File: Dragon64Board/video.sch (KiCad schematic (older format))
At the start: 69 parts, among them IC10 6847, IC12 74LS393, IC13 74LS32, IC14 74LS74, IC17 LM1889N, IC18 74LS86, IC19 74LS00, IC23 74LS393, IC24 74LS390, IC28 LM318N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

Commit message: PAL to NTSC
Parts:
- removed C20, C33, C44: 4.7uf tant, Capacitor_THT:CP_Radial_D4.0mm_P2.00mm, symbol Device:C_Polarized_US
- removed C32: 2-22p, dragon64:C_Trimmer_D7.5mm, symbol Device:C_Variable
- removed C36: 180p, Capacitor_THT:C_Disc_D7.5mm_W2.5mm_P5.00mm, symbol Device:C
- removed C48: .01u, Capacitor_THT:C_Disc_D7.5mm_W2.5mm_P5.00mm, symbol Device:C
- removed C49: 4p7, Capacitor_THT:C_Disc_D7.5mm_W2.5mm_P5.00mm, symbol Device:C
- removed C54: 330p, Capacitor_THT:C_Disc_D7.5mm_W2.5mm_P5.00mm, symbol Device:C
- removed D21, D22: 1N4148, Diode_THT:D_DO-35_SOD27_P7.62mm_Horizontal, symbol Device:D
- removed IC12, IC23: 74LS393, Package_DIP:DIP-14_W7.62mm_Socket_LongPads, symbol 74xx:74LS393
- removed IC13: 74LS32, Package_DIP:DIP-14_W7.62mm_Socket_LongPads, symbol 74xx:74LS32
- removed IC14, IC30: 74LS74, Package_DIP:DIP-14_W7.62mm_Socket_LongPads, symbol 74xx:74LS74
- removed IC17: LM1889N, Package_DIP:DIP-18_W7.62mm_Socket_LongPads, symbol dragon64:LM1889N
- removed IC18: 74LS86, Package_DIP:DIP-14_W7.62mm_Socket_LongPads, symbol 74xx:74LS86
- removed IC19: 74LS00, Package_DIP:DIP-14_W7.62mm_Socket_LongPads, symbol 74xx:74LS00
- removed IC24: 74LS390, Package_DIP:DIP-16_W7.62mm_Socket_LongPads, symbol 74xx:74LS390
- removed IC28: LM318N, Package_DIP:DIP-8_W7.62mm_Socket_LongPads, symbol Amplifier_Operational:LM318N
- removed IC29: 4053, Package_DIP:DIP-16_W7.62mm_Socket_LongPads, symbol dragon64:4053
- removed IC31: 74LS123, Package_DIP:DIP-16_W7.62mm_Socket_LongPads, symbol 74xx:74LS123
- removed IC9: 74LS20, Package_DIP:DIP-14_W7.62mm_Socket_LongPads, symbol 74xx:74LS20
- removed LK2: ~, Connector_PinHeader_2.54mm:PinHeader_1x03_P2.54mm_Vertical, symbol Jumper:Jumper_3_Bridged12
- removed R41, R58: 1K2, Resistor_THT:R_Axial_DIN0207_L6.3mm_D2.5mm_P7.62mm_Horizontal, symbol Device:R
- removed R42: 5K6, Resistor_THT:R_Axial_DIN0207_L6.3mm_D2.5mm_P7.62mm_Horizontal, symbol Device:R
- removed R43: 10R, Resistor_THT:R_Axial_DIN0207_L6.3mm_D2.5mm_P7.62mm_Horizontal, symbol Device:R
- removed R44: 680R, Resistor_THT:R_Axial_DIN0207_L6.3mm_D2.5mm_P7.62mm_Horizontal, symbol Device:R
- removed R45, R50, R51: 1K, Resistor_THT:R_Axial_DIN0207_L6.3mm_D2.5mm_P7.62mm_Horizontal, symbol Device:R
- removed R46: 270R, Resistor_THT:R_Axial_DIN0207_L6.3mm_D2.5mm_P7.62mm_Horizontal, symbol Device:R
- removed R47: 470R, Resistor_THT:R_Axial_DIN0207_L6.3mm_D2.5mm_P7.62mm_Horizontal, symbol Device:R
- removed R48: 220R, Resistor_THT:R_Axial_DIN0207_L6.3mm_D2.5mm_P7.62mm_Horizontal, symbol Device:R
- removed R49: 330R, Resistor_THT:R_Axial_DIN0207_L6.3mm_D2.5mm_P7.62mm_Horizontal, symbol Device:R
- removed R52, R57: 3K3, Resistor_THT:R_Axial_DIN0207_L6.3mm_D2.5mm_P7.62mm_Horizontal, symbol Device:R
- removed R53, R56: 2K7, Resistor_THT:R_Axial_DIN0207_L6.3mm_D2.5mm_P7.62mm_Horizontal, symbol Device:R
- removed R54, R55: 10K, Resistor_THT:R_Axial_DIN0207_L6.3mm_D2.5mm_P7.62mm_Horizontal, symbol Device:R
- removed R59: 6K8, Resistor_THT:R_Axial_DIN0207_L6.3mm_D2.5mm_P7.62mm_Horizontal, symbol Device:R
- removed R60: 15K, Resistor_THT:R_Axial_DIN0207_L6.3mm_D2.5mm_P7.62mm_Horizontal, symbol Device:R
- removed R61: 1K8, Resistor_THT:R_Axial_DIN0207_L6.3mm_D2.5mm_P7.62mm_Horizontal, symbol Device:R
- removed R62: 8K2, Resistor_THT:R_Axial_DIN0207_L6.3mm_D2.5mm_P7.62mm_Horizontal, symbol Device:R
- removed R63: 12K, Resistor_THT:R_Axial_DIN0207_L6.3mm_D2.5mm_P7.62mm_Horizontal, symbol Device:R
- removed R72: 22K, Resistor_THT:R_Axial_DIN0207_L6.3mm_D2.5mm_P7.62mm_Horizontal, symbol Device:R
- removed TR2, TR3: 2N2369A, Package_TO_SOT_THT:TO-18-3, symbol Device:Q_NPN_EBC
- removed TR4: BC212L, Package_TO_SOT_THT:TO-92, symbol Device:Q_PNP_ECB
- removed VR1: 10k, Potentiometer_THT:Potentiometer_Vishay_T7-YA_Single_Vertical, symbol Device:R_Potentiometer
- removed Y3: 4.433619Mhz, Crystal:Crystal_HC49-U_Vertical, symbol Device:Crystal
- added C20, C32: .01u, Capacitor_THT:C_Disc_D7.5mm_W2.5mm_P5.00mm, symbol Device:C
- added C33: 0.1uf, Capacitor_THT:C_Disc_D7.5mm_W2.5mm_P5.00mm, symbol Device:C
- added C36: 100uf, Capacitor_THT:CP_Radial_D4.0mm_P2.00mm, symbol Device:C_Polarized_US
- added C44: 470pf, Capacitor_THT:C_Disc_D7.5mm_W2.5mm_P5.00mm, symbol Device:C
- added D4: 1N4002, Diode_THT:D_DO-35_SOD27_P7.62mm_Horizontal, symbol Device:D
- added J3: composite on luma, Connector_PinHeader_2.54mm:PinHeader_1x02_P2.54mm_Vertical, symbol Connector:Conn_01x02_Male
- added Q1: BC557, Package_TO_SOT_THT:TO-92_Wide, symbol Device:Q_PNP_BCE
- added Q2, Q3: 2N2222, Package_TO_SOT_THT:TO-18-3, symbol Device:Q_NPN_BCE
- added R11: 10K, Resistor_THT:R_Axial_DIN0207_L6.3mm_D2.5mm_P7.62mm_Horizontal, symbol Device:R
- added R12, R7: 390, Resistor_THT:R_Axial_DIN0207_L6.3mm_D2.5mm_P7.62mm_Horizontal, symbol Device:R
- added R13: 820, Resistor_THT:R_Axial_DIN0207_L6.3mm_D2.5mm_P7.62mm_Horizontal, symbol Device:R
- added R30: 420, Resistor_THT:R_Axial_DIN0207_L6.3mm_D2.5mm_P7.62mm_Horizontal, symbol Device:R
- added R31, R6: 470, Resistor_THT:R_Axial_DIN0207_L6.3mm_D2.5mm_P7.62mm_Horizontal, symbol Device:R
- added R8: 5.6k, Resistor_THT:R_Axial_DIN0207_L6.3mm_D2.5mm_P7.62mm_Horizontal, symbol Device:R
- added U2: MC1372, Package_DIP:DIP-14_W7.62mm_LongPads, symbol New_Library:MC1372
- C21: value 3p3 -> .01u
- C29, C31: value 33p -> .01u
- C30: value .1u -> 56pf
- C35: value 180p -> 25uf
- C37: value 180p -> 390pf
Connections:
- net labels added: CHROMA, DA0, FS, HS, LUMA, VCLK1
- net labels removed: -5V, CMP, DA0', E, MOD, VID+5V, VIDEO, ~FS, ~HS, ~NHS
- wire segments 439 -> 143
- no-connect marks 41 -> 18
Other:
- note removed: "*"
- note removed: "LINE PULSES"
- note removed: "TANT"
- moved on the sheet: C34, C38, C41, C45, C50, C51

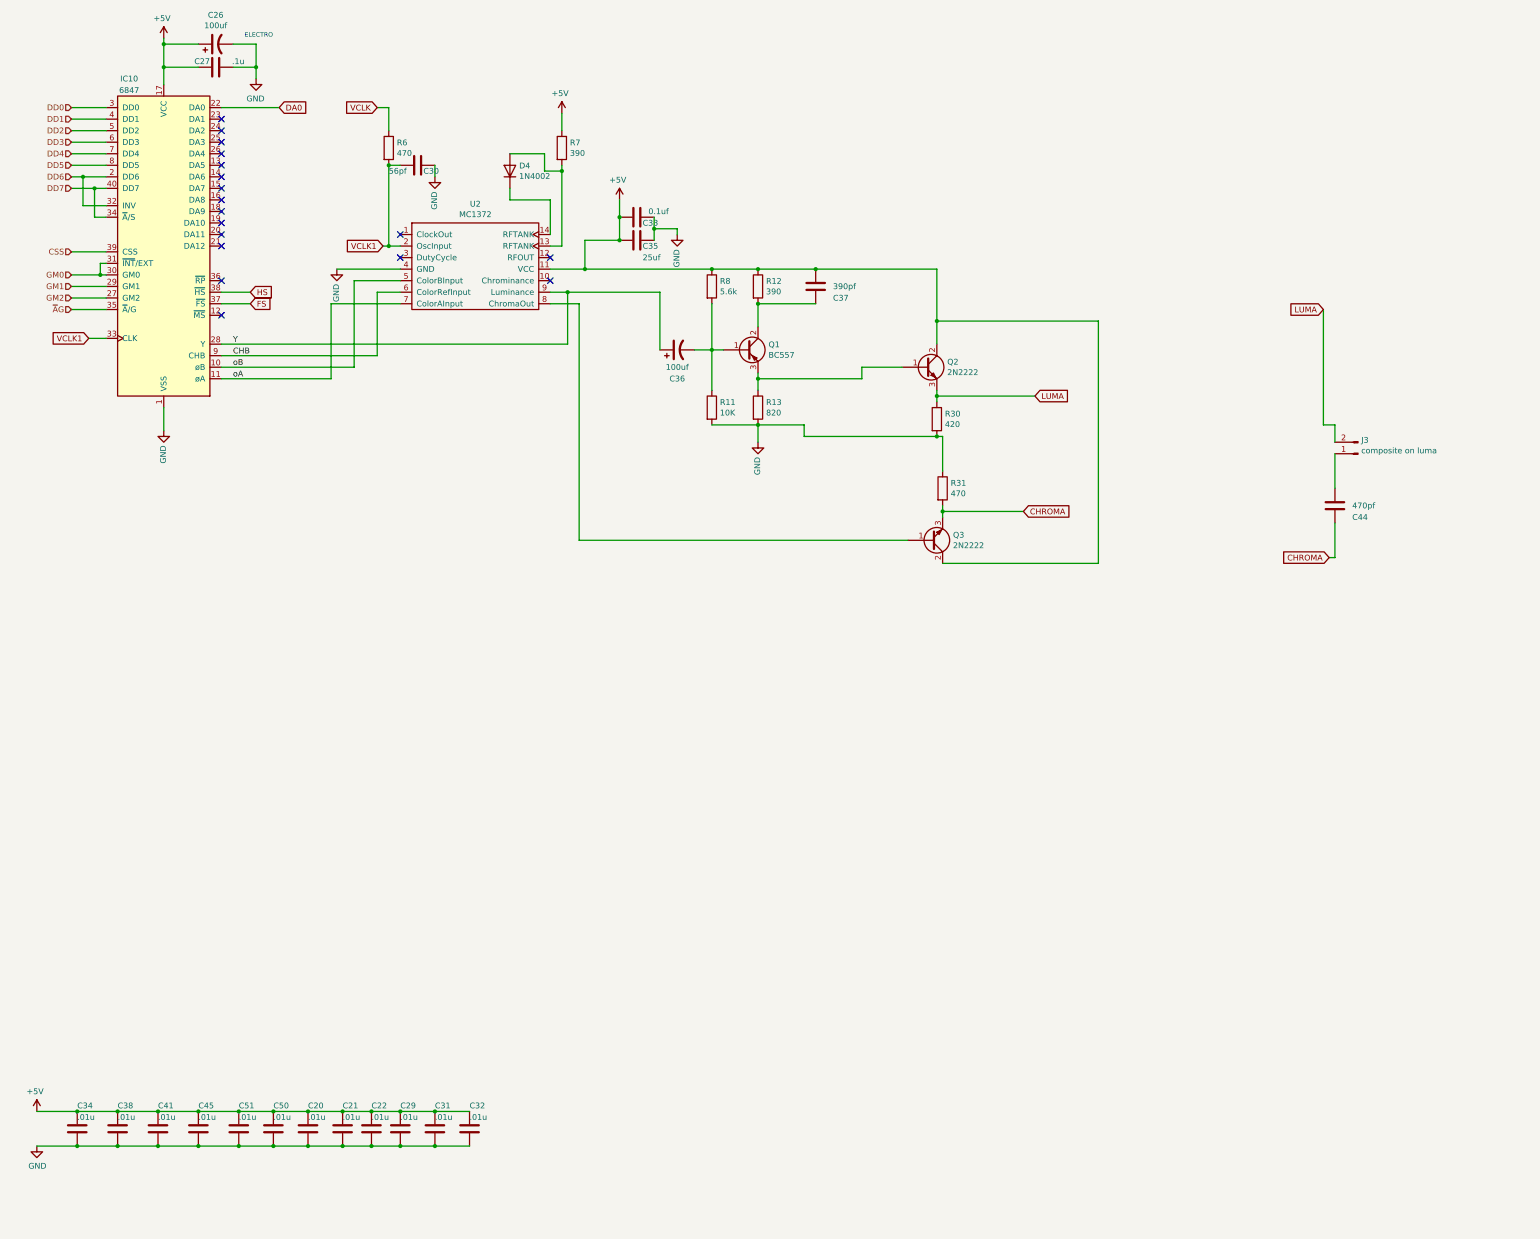
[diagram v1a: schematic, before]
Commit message: Bug fixes and add Floppy Controller
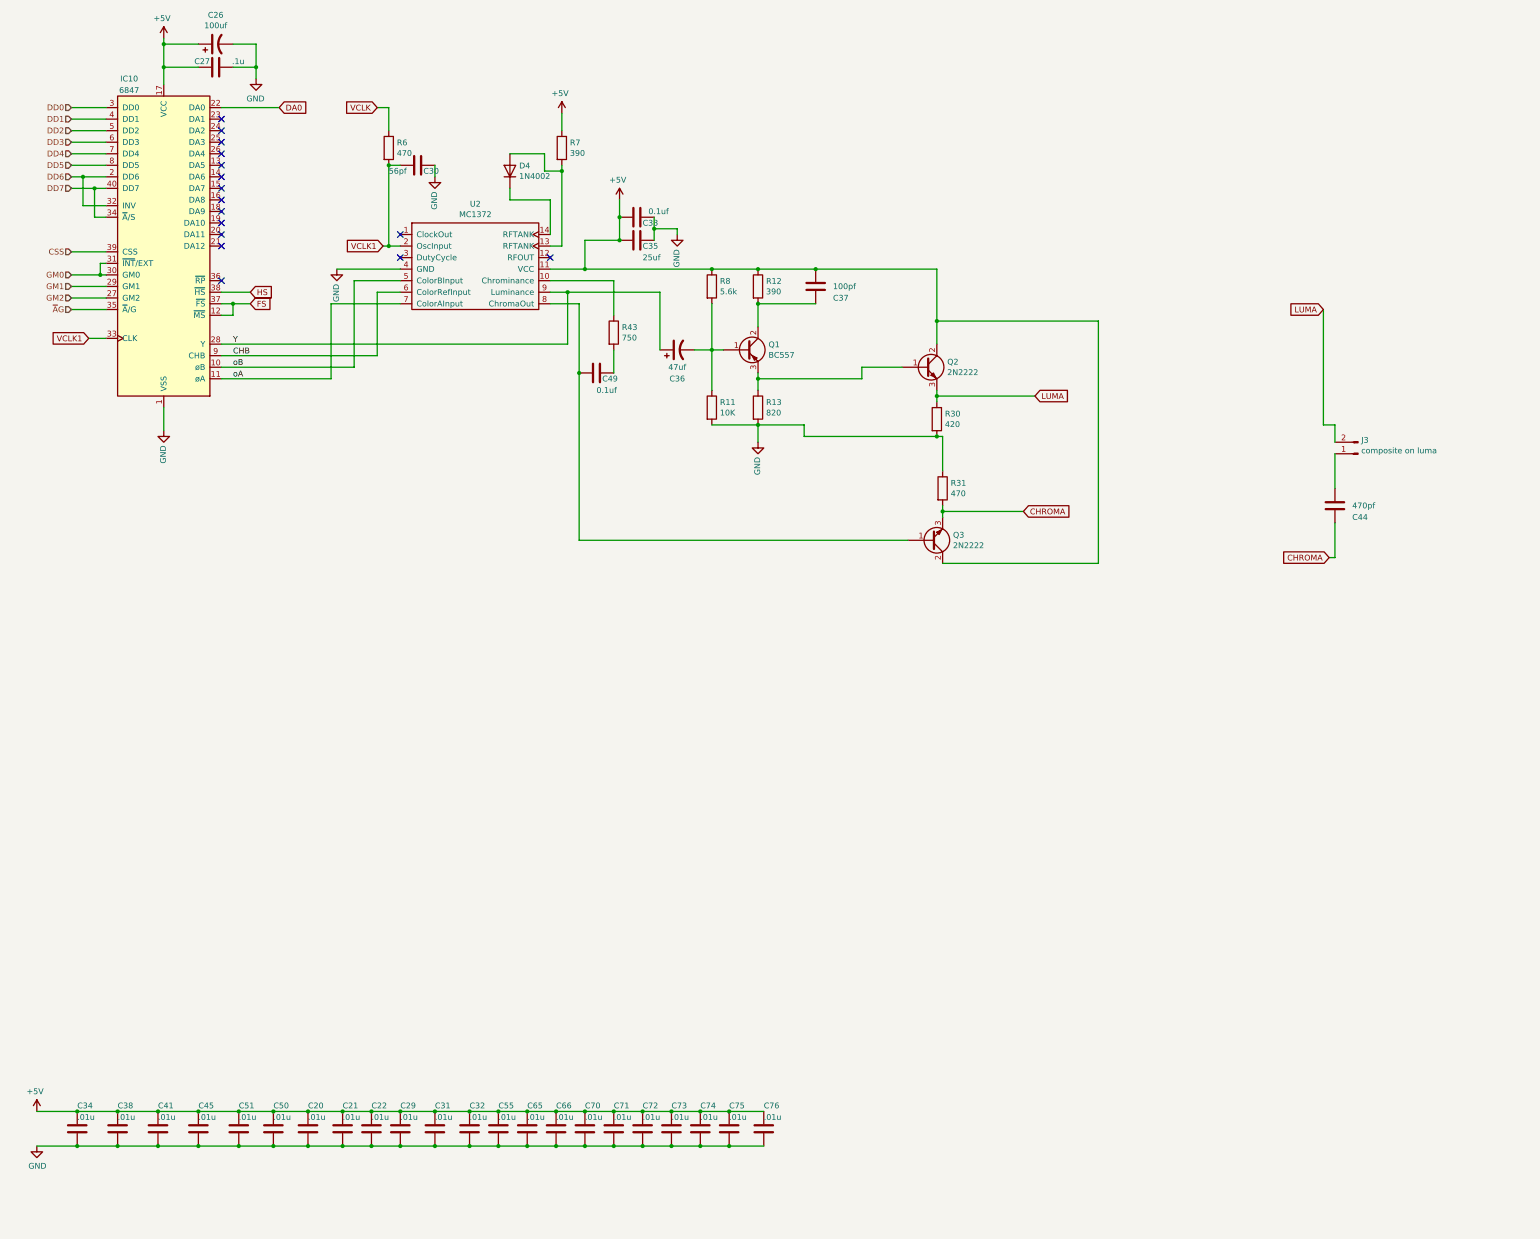
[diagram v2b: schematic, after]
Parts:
- added C49: 0.1uf, Capacitor_THT:C_Disc_D7.5mm_W2.5mm_P5.00mm, symbol Device:C
- added C55, C65, C66, C70, C71, C72, C73, C74, C75, C76: .01u, Capacitor_THT:C_Disc_D7.5mm_W2.5mm_P5.00mm, symbol Device:C
- added R43: 750, Resistor_THT:R_Axial_DIN0207_L6.3mm_D2.5mm_P7.62mm_Horizontal, symbol Device:R
- C36: value 100uf -> 47uf
- C37: value 390pf -> 100pf
- Q1: footprint Package_TO_SOT_THT:TO-92_Wide -> logo:TO-92_HandSolder_FIXED
- Q2, Q3: footprint Package_TO_SOT_THT:TO-18-3 -> logo:TO-18-3_FIXED
- U2: footprint Package_DIP:DIP-14_W7.62mm_LongPads -> Package_DIP:DIP-14_W7.62mm_Socket_LongPads
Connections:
- net +5V: now also C55.1, C65.1, C66.1, C70.1, C71.1, C72.1, C73.1, C74.1, C75.1, C76.1
- net FS: now also IC10.12 (~MS~)
- net GND: now also C55.2, C65.2, C66.2, C70.2, C71.2, C72.2, C73.2, C74.2, C75.2, C76.2
- net at U2.10 (Chrominance): now also R43.1
- net at Q3.1 (B), U2.8 (ChromaOut): now also C49.1
- new net: C49.2, R43.2
- no-connect marks 18 -> 16
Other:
- note removed: "ELECTRO"
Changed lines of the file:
@@
 $Descr A3 16535 11693
 encoding utf-8
-Sheet 3 5
-Title "Dragon CPU 64K (PAL)"
-Date "2020-12-21"
+Sheet 3 6
+Title "Dragon CPU 64K"
+Date "2022-04-09"
 Rev "4"
-Comp "Dragon Data Ltd."
-Comment1 "Transcribed by Ciaran Anscomb, 2020"
-Comment2 "Video, including PAL logic"
+Comp "Originally by Dragon Data Ltd."
+Comment1 ""
+Comment2 ""
 Comment3 ""
 Comment4 ""
@@
 	-1   0    0    -1
 $EndComp
-NoConn ~ 2200 3150
 $Comp
 L power:GND #PWR?
@@
 	-1   0    0    -1
 $EndComp
-Text Notes 2400 750  0    39   ~ 0
-ELECTRO
 $Comp
 L Device:C_Polarized_US C26
@@
 F 0 "U2" H 4400 2515 50  0000 C CNN
 F 1 "MC1372" H 4400 2424 50  0000 C CNN
-F 2 "Package_DIP:DIP-14_W7.62mm_LongPads" H 4950 2350 50  0001 C CNN
+F 2 "Package_DIP:DIP-14_W7.62mm_Socket_LongPads" H 4950 2350 50  0001 C CNN
 F 3 "" H 4950 2350 50  0001 C CNN
 	1    4100 2350
@@
 F 0 "Q2" H 8490 3646 50  0000 L CNN
 F 1 "2N2222" H 8490 3555 50  0000 L CNN
-F 2 "Package_TO_SOT_THT:TO-18-3" H 8500 3700 50  0001 C CNN
+F 2 "logo:TO-18-3_FIXED" H 8500 3700 50  0001 C CNN
 F 3 "~" H 8300 3600 50  0001 C CNN
 	1    8300 3600
@@
 P 6150 3450
 F 0 "C36" V 5900 3450 50  0000 C CNN
-F 1 "100uf" V 6000 3450 50  0000 C CNN
+F 1 "47uf" V 6000 3450 50  0000 C CNN
 F 2 "Capacitor_THT:CP_Radial_D4.0mm_P2.00mm" H 6150 3450 50  0001 C CNN
 F 3 "~" H 6150 3450 50  0001 C CNN
@@
 Wire Wire Line
 	5350 2750 6450 2750
-NoConn ~ 5050 2850
 Wire Wire Line
 	5200 2950 6000 2950
@@
 P 7350 2900
 F 0 "C37" H 7200 2800 50  0000 R CNN
-F 1 "390pf" H 7200 2900 50  0000 R CNN
+F 1 "100pf" H 7200 2900 50  0000 R CNN
 F 2 "Capacitor_THT:C_Disc_D7.5mm_W2.5mm_P5.00mm" H 7388 2750 50  0001 C CNN
 F 3 "~" H 7350 2900 50  0001 C CNN
@@
 F 0 "Q1" H 6941 3496 50  0000 L CNN
 F 1 "BC557" H 6941 3405 50  0000 L CNN
-F 2 "Package_TO_SOT_THT:TO-92_Wide" H 6950 3550 50  0001 C CNN
+F 2 "logo:TO-92_HandSolder_FIXED" H 6950 3550 50  0001 C CNN
 F 3 "~" H 6750 3450 50  0001 C CNN
 	1    6750 3450
@@
 F 0 "Q3" H 8540 5054 50  0000 L CNN
 F 1 "2N2222" H 8540 5145 50  0000 L CNN
-F 2 "Package_TO_SOT_THT:TO-18-3" H 8550 5200 50  0001 C CNN
+F 2 "logo:TO-18-3_FIXED" H 8550 5200 50  0001 C CNN
 F 3 "~" H 8350 5100 50  0001 C CNN
 	1    8350 5100
@@
 	5300 5100 8150 5100
 Wire Wire Line
-	5300 3050 5300 5100
+	5300 3050 5300 3650
 $Comp
 L Device:R R31
@@
 FS
 Wire Wire Line
-	2200 3050 2450 3050
+	2200 3050 2300 3050
 Text GLabel 2700 1350 2    50   Input ~ 0
 DA0
+Wire Wire Line
+	2200 3150 2300 3150
+Wire Wire Line
+	2300 3150 2300 3050
+Connection ~ 2300 3050
+Wire Wire Line
+	2300 3050 2450 3050
+$Comp
+L Device:C C49
+U 1 1 62A76B63
+P 5450 3650
+F 0 "C49" V 5500 3600 50  0000 R CNN
+F 1 "0.1uf" V 5600 3650 50  0000 R CNN
+F 2 "Capacitor_THT:C_Disc_D7.5mm_W2.5mm_P5.00mm" H 5488 3500 50  0001 C CNN
+F 3 "~" H 5450 3650 50  0001 C CNN
+	1    5450 3650
+	0    -1   1    0
+$EndComp
+Connection ~ 5300 3650
+Wire Wire Line
+	5300 3650 5300 5100
+$Comp
+L Device:R R43
+U 1 1 62A77624
+P 5600 3300
+F 0 "R43" H 5670 3346 50  0000 L CNN
+F 1 "750" H 5670 3255 50  0000 L CNN
+F 2 "Resistor_THT:R_Axial_DIN0207_L6.3mm_D2.5mm_P7.62mm_Horizontal" V 5530 3300 50  0001 C CNN
+F 3 "~" H 5600 3300 50  0001 C CNN
+	1    5600 3300
+	1    0    0    -1
+$EndComp
+Wire Wire Line
+	5600 3650 5600 3450
+Wire Wire Line
+	5600 3150 5600 2850
+Wire Wire Line
+	5600 2850 5050 2850
+$Comp
+L Device:C C55
+U 1 1 62D48742
+P 4600 10200
+F 0 "C55" H 4600 10400 50  0000 R CNN
+F 1 ".01u" H 4600 10300 50  0000 R CNN
+F 2 "Capacitor_THT:C_Disc_D7.5mm_W2.5mm_P5.00mm" H 4638 10050 50  0001 C CNN
+F 3 "~" H 4600 10200 50  0001 C CNN
+	1    4600 10200
+	-1   0    0    -1
+$EndComp
+$Comp
+L Device:C C65
+U 1 1 62D48C92
+P 4850 10200
+F 0 "C65" H 4850 10400 50  0000 R CNN
+F 1 ".01u" H 4850 10300 50  0000 R CNN
+F 2 "Capacitor_THT:C_Disc_D7.5mm_W2.5mm_P5.00mm" H 4888 10050 50  0001 C CNN
+F 3 "~" H 4850 10200 50  0001 C CNN
+	1    4850 10200
+	-1   0    0    -1
+$EndComp
+$Comp
+L Device:C C66
+U 1 1 62D4920F
+P 5100 10200
+F 0 "C66" H 5100 10400 50  0000 R CNN
+F 1 ".01u" H 5100 10300 50  0000 R CNN
+F 2 "Capacitor_THT:C_Disc_D7.5mm_W2.5mm_P5.00mm" H 5138 10050 50  0001 C CNN
+F 3 "~" H 5100 10200 50  0001 C CNN
+	1    5100 10200
+	-1   0    0    -1
+$EndComp
+$Comp
+L Device:C C70
+U 1 1 62D49603
+P 5350 10200
+F 0 "C70" H 5350 10400 50  0000 R CNN
+F 1 ".01u" H 5350 10300 50  0000 R CNN
+F 2 "Capacitor_THT:C_Disc_D7.5mm_W2.5mm_P5.00mm" H 5388 10050 50  0001 C CNN
+F 3 "~" H 5350 10200 50  0001 C CNN
+	1    5350 10200
+	-1   0    0    -1
+$EndComp
+$Comp
+L Device:C C71
+U 1 1 62D499C0
+P 5600 10200
+F 0 "C71" H 5600 10400 50  0000 R CNN
+F 1 ".01u" H 5600 10300 50  0000 R CNN
+F 2 "Capacitor_THT:C_Disc_D7.5mm_W2.5mm_P5.00mm" H 5638 10050 50  0001 C CNN
+F 3 "~" H 5600 10200 50  0001 C CNN
+	1    5600 10200
+	-1   0    0    -1
+$EndComp
+$Comp
+L Device:C C72
+U 1 1 62D49EBE
+P 5850 10200
+F 0 "C72" H 5850 10400 50  0000 R CNN
+F 1 ".01u" H 5850 10300 50  0000 R CNN
+F 2 "Capacitor_THT:C_Disc_D7.5mm_W2.5mm_P5.00mm" H 5888 10050 50  0001 C CNN
+F 3 "~" H 5850 10200 50  0001 C CNN
+	1    5850 10200
+	-1   0    0    -1
+$EndComp
+$Comp
+L Device:C C73
+U 1 1 62D4A2D2
+P 6100 10200
+F 0 "C73" H 6100 10400 50  0000 R CNN
+F 1 ".01u" H 6100 10300 50  0000 R CNN
+F 2 "Capacitor_THT:C_Disc_D7.5mm_W2.5mm_P5.00mm" H 6138 10050 50  0001 C CNN
+F 3 "~" H 6100 10200 50  0001 C CNN
+	1    6100 10200
+	-1   0    0    -1
+$EndComp
+$Comp
+L Device:C C74
+U 1 1 62D4A6CE
+P 6350 10200
+F 0 "C74" H 6350 10400 50  0000 R CNN
+F 1 ".01u" H 6350 10300 50  0000 R CNN
+F 2 "Capacitor_THT:C_Disc_D7.5mm_W2.5mm_P5.00mm" H 6388 10050 50  0001 C CNN
+F 3 "~" H 6350 10200 50  0001 C CNN
+	1    6350 10200
+	-1   0    0    -1
+$EndComp
+$Comp
+L Device:C C75
+U 1 1 62D4B1B4
+P 6600 10200
+F 0 "C75" H 6600 10400 50  0000 R CNN
+F 1 ".01u" H 6600 10300 50  0000 R CNN
+F 2 "Capacitor_THT:C_Disc_D7.5mm_W2.5mm_P5.00mm" H 6638 10050 50  0001 C CNN
+F 3 "~" H 6600 10200 50  0001 C CNN
+	1    6600 10200
+	-1   0    0    -1
+$EndComp
+$Comp
+L Device:C C76
+U 1 1 62D4B4E5
+P 6900 10200
+F 0 "C76" H 6900 10400 50  0000 R CNN
+F 1 ".01u" H 6900 10300 50  0000 R CNN
+F 2 "Capacitor_THT:C_Disc_D7.5mm_W2.5mm_P5.00mm" H 6938 10050 50  0001 C CNN
+F 3 "~" H 6900 10200 50  0001 C CNN
+	1    6900 10200
+	-1   0    0    -1
+$EndComp
+Wire Wire Line
+	4350 10350 4600 10350
+Connection ~ 4350 10350
+Wire Wire Line
+	4600 10350 4850 10350
+Connection ~ 4600 10350
+Wire Wire Line
+	4850 10350 5100 10350
+Connection ~ 4850 10350
+Wire Wire Line
+	5100 10350 5350 10350
+Connection ~ 5100 10350
+Wire Wire Line
+	5350 10350 5600 10350
+Connection ~ 5350 10350
+Wire Wire Line
+	5600 10350 5850 10350
+Connection ~ 5600 10350
+Wire Wire Line
+	5850 10350 6100 10350
+Connection ~ 5850 10350
+Wire Wire Line
+	6100 10350 6350 10350
+Connection ~ 6100 10350
+Wire Wire Line
+	6350 10350 6600 10350
+Connection ~ 6350 10350
+Wire Wire Line
+	6600 10350 6900 10350
+Connection ~ 6600 10350
+Wire Wire Line
+	6900 10050 6600 10050
+Wire Wire Line
+	6600 10050 6350 10050
+Connection ~ 6600 10050
+Wire Wire Line
+	6350 10050 6100 10050
+Connection ~ 6350 10050
+Wire Wire Line
+	6100 10050 5850 10050
+Connection ~ 6100 10050
+Wire Wire Line
+	5850 10050 5600 10050
+Connection ~ 5850 10050
+Wire Wire Line
+	5600 10050 5350 10050
+Connection ~ 5600 10050
+Wire Wire Line
+	5350 10050 5100 10050
+Connection ~ 5350 10050
+Wire Wire Line
+	5100 10050 4850 10050
+Connection ~ 5100 10050
+Wire Wire Line
+	4850 10050 4600 10050
+Connection ~ 4850 10050
+Wire Wire Line
+	4600 10050 4350 10050
+Connection ~ 4600 10050
+Connection ~ 4350 10050
 $EndSCHEMATC
